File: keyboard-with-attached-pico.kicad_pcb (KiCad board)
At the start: 2 copper layers, 229.6 x 81.8 mm, 98 parts

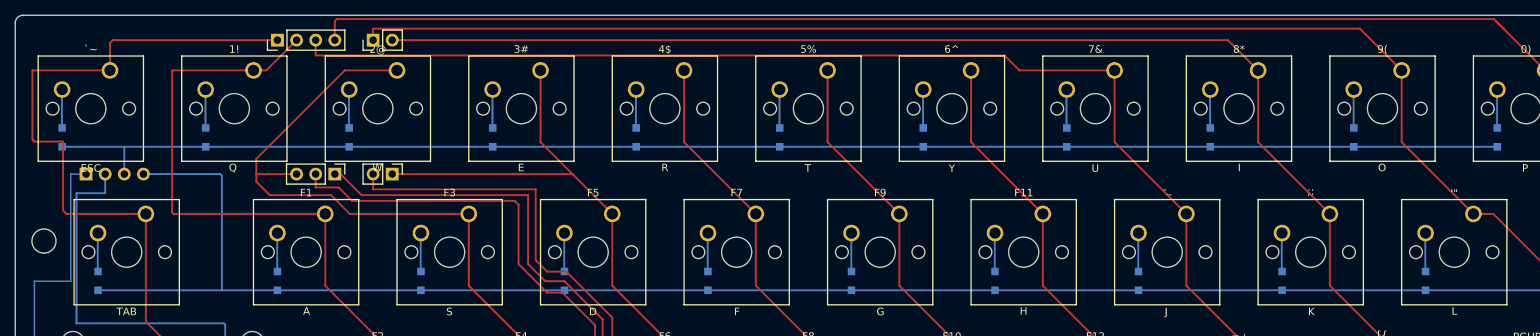
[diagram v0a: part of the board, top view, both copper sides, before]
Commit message: Updated board and firmware with new routing, makes sure the Pi Pico is facing the right way
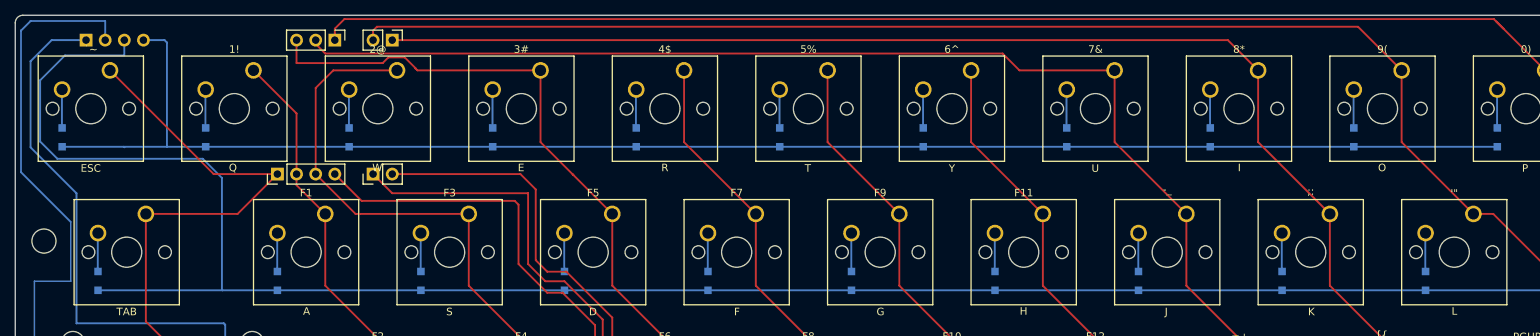
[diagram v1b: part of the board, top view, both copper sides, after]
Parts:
- moved REF** 17.8 mm to (144.8, 133.6)
- moved REF** 17.8 mm to (132.1, 133.6)
- moved REF** 17.8 mm to (139.7, 115.8)
- moved REF** 17.8 mm to (147.3, 115.8)
- moved REF** 17.8 mm to (106.7, 115.8)
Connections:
- REF** pad 1: /Col_9 -> /Col_5
- REF** pad 2: /Col_8 -> /Col_4
- REF** pad 3: /Col_7 -> /Col_2
- REF** pad 4: /Col_10 -> /Col_6
- REF** pad 1: /Col_5 -> /Col_10
- REF** pad 2: /Col_6 -> /Col_7
- REF** pad 3: /Col_2 -> /Col_3
- REF** pad 1: /Col_3 -> /Col_8
- REF** pad 2: /Col_4 -> /Col_9
- REF** pad 1: /Row_3 -> /Row_2
- REF** pad 2: /Row_2 -> /Row_3
- REF** pad 3: /Row_0 -> /Row_1
- REF** pad 4: /Row_1 -> /Row_0
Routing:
- net /Row_1: track 225.7 -> 263.8 mm
- net /Col_1: track 110.9 -> 76.5 mm
- net /Row_3: track 345.5 -> 379.5 mm
- net /Col_0: track 114.0 -> 91.6 mm
- net /Row_2: track 257.9 -> 280.2 mm
- net /Col_2: track 115.3 -> 99.1 mm
- net /Row_0: track 194.2 -> 207.7 mm
- net /Col_3: track 93.1 -> 105.6 mm
- net /Col_5: track 225.9 -> 220.9 mm
- net /Col_4: track 188.4 -> 184.7 mm
- net /Col_6: track 259.6 -> 256.8 mm
- net /Col_7: track 184.3 -> 183.4 mm
- net /Col_10: track 232.5 -> 231.9 mm

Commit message: Updated v1.01 and ready for production
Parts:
- D1, D10, D11, D12, D13, D14, D15, D16, D17, D18, D19, D2, D20, D21, D22, D23, D24, D25, D26, D27, D28, D29, D3, D30, D31, D32, D33, D35, D36, D37, D38, D39, D4, D40, D41, D42, D43, D5, D6, D7, D8, D9, locked (x2): footprint Diode_SMD:D_SOD-323_HandSoldering -> Diode_SMD:D_SMA_Handsoldering
- moved D2 2.59 mm to (139.1, 129.4), turned to 0 degrees
- moved D12 2.49 mm to (108.3, 150.3)
- moved D13 2.49 mm to (132.1, 150.3)
- moved D14 2.49 mm to (151.1, 150.3)
- moved D15 2.49 mm to (170.2, 150.3)
- moved D16 2.49 mm to (189.2, 150.3)
- moved D17 2.49 mm to (208.3, 150.3)
- moved D18 2.49 mm to (227.3, 150.3)
- moved D19 2.49 mm to (246.4, 150.3)
- moved D20 2.49 mm to (265.4, 150.3)
- moved D21 2.49 mm to (284.5, 150.3)
- moved D22 2.49 mm to (308.3, 150.3)
- moved D33 2.23 mm to (313.1, 169.1)
- moved D23 2.23 mm to (113.0, 169.1)
- moved D24 2.23 mm to (141.6, 169.1)
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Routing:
- net /Row_3: track 379.5 -> 399.6 mm
- net /Row_1: track 263.8 -> 275.3 mm
- net /Row_0: track 207.7 -> 215.5 mm
- net /Row_2: track 280.2 -> 275.8 mm
- net Net-(D2-Pad2): track 5.23 -> 6.98 mm
- net Net-(D12-Pad2): track 5.23 -> 6.34 mm
- net Net-(D22-Pad2): track 5.23 -> 6.34 mm
- net Net-(D21-Pad2): track 5.23 -> 6.34 mm
- net Net-(D20-Pad2): track 5.23 -> 6.34 mm
- net Net-(D19-Pad2): track 5.23 -> 6.34 mm
- net Net-(D18-Pad2): track 5.23 -> 6.34 mm
- net Net-(D17-Pad2): track 5.23 -> 6.34 mm
- net Net-(D16-Pad2): track 5.23 -> 6.34 mm
- net Net-(D15-Pad2): track 5.23 -> 6.34 mm
- net Net-(D14-Pad2): track 5.23 -> 6.34 mm
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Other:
- rule pad_to_mask_clearance: 0.051 -> 0
